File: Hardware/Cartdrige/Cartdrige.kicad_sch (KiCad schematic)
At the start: 5 parts, among them J1 CARTDRIGE, U1 28C256, U2 28C256

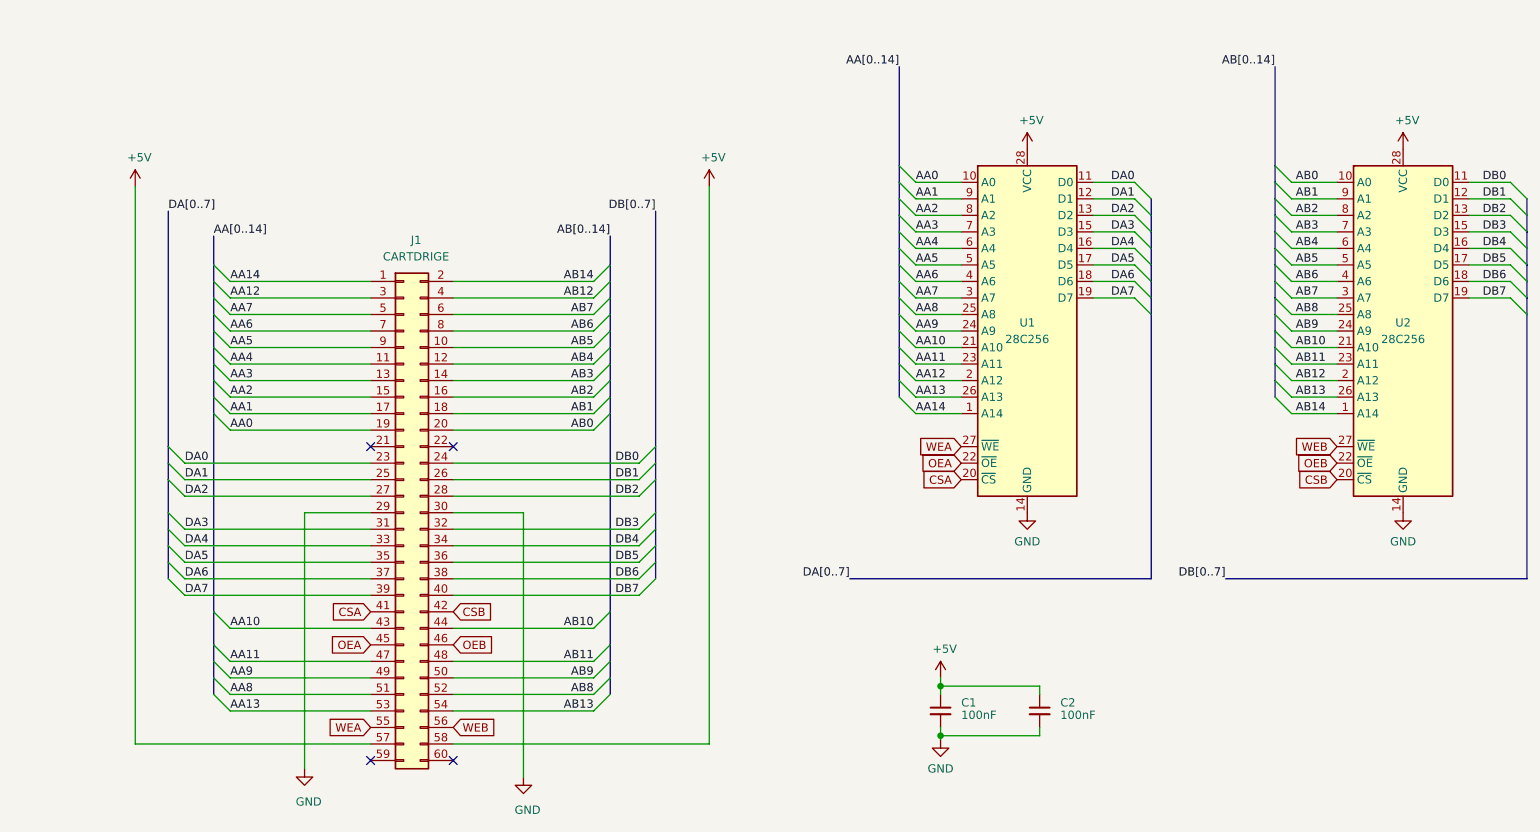
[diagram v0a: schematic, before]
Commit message: implement graphic loading from ROM
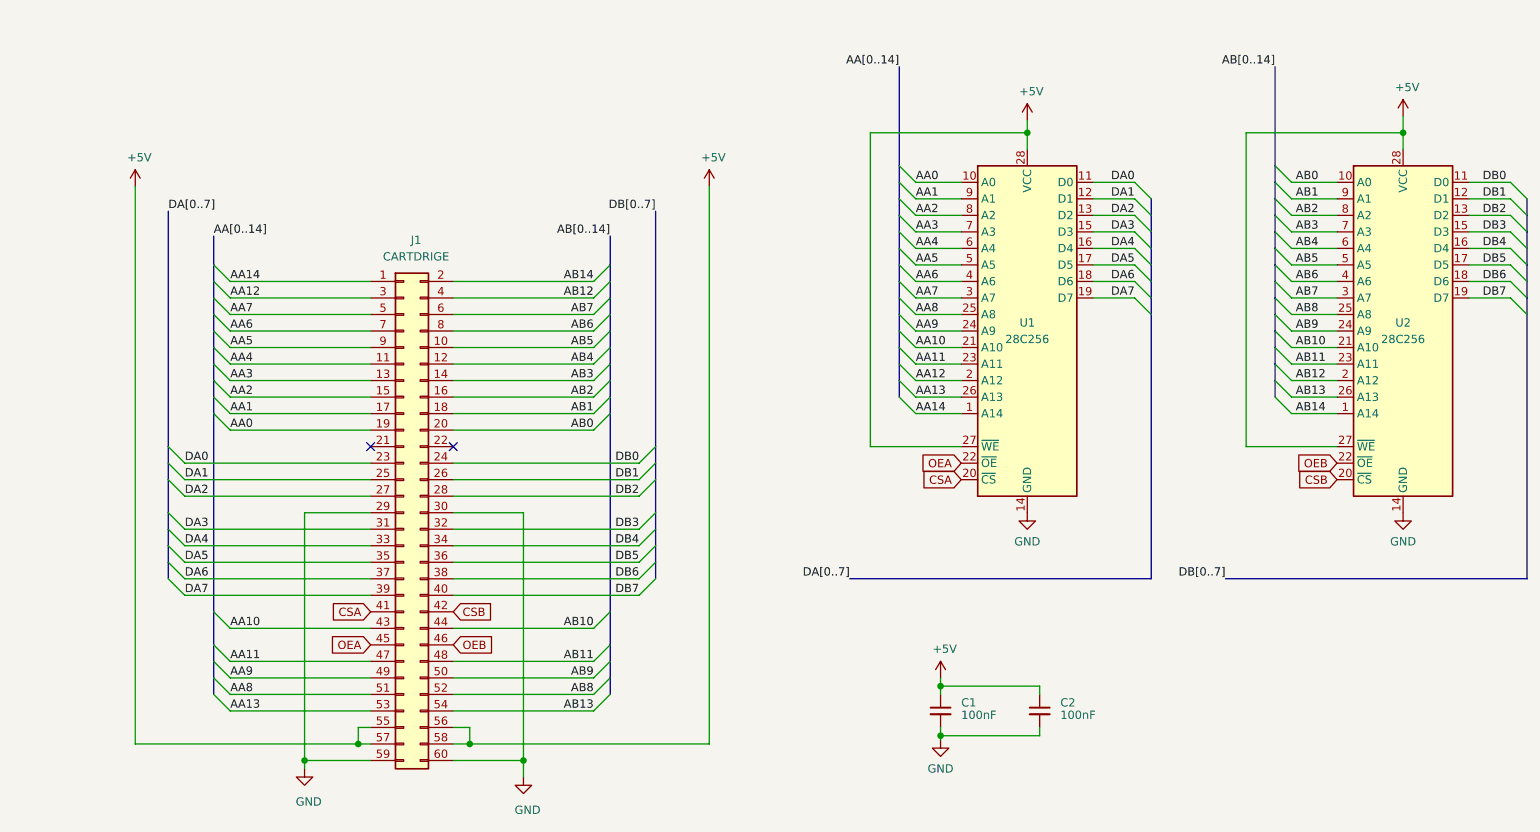
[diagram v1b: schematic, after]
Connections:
- net WEA is gone; now on net +5V: J1.55 (Pin_55), U1.27 (~WE)
- net WEB is gone; now on net +5V: J1.56 (Pin_56), U2.27 (~WE)
- net GND: now also J1.59 (Pin_59), J1.60 (Pin_60)
- no-connect marks 4 -> 2
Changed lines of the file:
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@@
 (kicad_sch (version 20201015) (generator eeschema)
   (paper "A4")
+  (junction (at 65.405 131.445) (diameter 1.016) (color 0 0 0 0))
+  (junction (at 73.66 128.905) (diameter 1.016) (color 0 0 0 0))
+  (junction (at 90.805 128.905) (diameter 1.016) (color 0 0 0 0))
+  (junction (at 99.06 131.445) (diameter 1.016) (color 0 0 0 0))
   (junction (at 163.195 120.015) (diameter 1.016) (color 0 0 0 0))
   (junction (at 163.195 127.635) (diameter 1.016) (color 0 0 0 0))
+  (junction (at 176.53 34.925) (diameter 1.016) (color 0 0 0 0))
+  (junction (at 234.315 34.925) (diameter 1.016) (color 0 0 0 0))
+  (no_connect (at 88.265 83.185))
   (no_connect (at 75.565 83.185))
-  (no_connect (at 88.265 83.185))
-  (no_connect (at 88.265 131.445))
-  (no_connect (at 75.565 131.445))
   (bus_entry (at 46.99 85.725) (size -2.54 -2.54)
     (stroke (width 0.1524) (type solid) (color 0 0 0 0))
@@
     (stroke (width 0) (type solid) (color 0 0 0 0))
   )
-  (wire (pts (xy 39.37 128.905) (xy 75.565 128.905))
+  (wire (pts (xy 39.37 128.905) (xy 73.66 128.905))
     (stroke (width 0) (type solid) (color 0 0 0 0))
   )
@@
     (stroke (width 0) (type solid) (color 0 0 0 0))
   )
-  (wire (pts (xy 65.405 93.345) (xy 65.405 132.715))
+  (wire (pts (xy 65.405 93.345) (xy 65.405 131.445))
     (stroke (width 0) (type solid) (color 0 0 0 0))
   )
@@
     (stroke (width 0) (type solid) (color 0 0 0 0))
   )
+  (wire (pts (xy 65.405 131.445) (xy 65.405 132.715))
+    (stroke (width 0) (type solid) (color 0 0 0 0))
+  )
+  (wire (pts (xy 65.405 131.445) (xy 75.565 131.445))
+    (stroke (width 0) (type solid) (color 0 0 0 0))
+  )
+  (wire (pts (xy 73.66 126.365) (xy 73.66 128.905))
+    (stroke (width 0) (type solid) (color 0 0 0 0))
+  )
+  (wire (pts (xy 73.66 128.905) (xy 75.565 128.905))
+    (stroke (width 0) (type solid) (color 0 0 0 0))
+  )
+  (wire (pts (xy 75.565 126.365) (xy 73.66 126.365))
+    (stroke (width 0) (type solid) (color 0 0 0 0))
+  )
   (wire (pts (xy 88.265 57.785) (xy 109.855 57.785))
     (stroke (width 0) (type solid) (color 0 0 0 0))
@@
     (stroke (width 0) (type solid) (color 0 0 0 0))
   )
-  (wire (pts (xy 88.265 128.905) (xy 127.635 128.905))
-    (stroke (width 0) (type solid) (color 0 0 0 0))
-  )
-  (wire (pts (xy 99.06 93.345) (xy 99.06 133.985))
+  (wire (pts (xy 88.265 126.365) (xy 90.805 126.365))
+    (stroke (width 0) (type solid) (color 0 0 0 0))
+  )
+  (wire (pts (xy 88.265 128.905) (xy 90.805 128.905))
+    (stroke (width 0) (type solid) (color 0 0 0 0))
+  )
+  (wire (pts (xy 88.265 131.445) (xy 99.06 131.445))
+    (stroke (width 0) (type solid) (color 0 0 0 0))
+  )
+  (wire (pts (xy 90.805 126.365) (xy 90.805 128.905))
+    (stroke (width 0) (type solid) (color 0 0 0 0))
+  )
+  (wire (pts (xy 90.805 128.905) (xy 127.635 128.905))
+    (stroke (width 0) (type solid) (color 0 0 0 0))
+  )
+  (wire (pts (xy 99.06 93.345) (xy 99.06 131.445))
+    (stroke (width 0) (type solid) (color 0 0 0 0))
+  )
+  (wire (pts (xy 99.06 131.445) (xy 99.06 133.985))
     (stroke (width 0) (type solid) (color 0 0 0 0))
   )
@@
     (stroke (width 0) (type solid) (color 0 0 0 0))
   )
+  (wire (pts (xy 152.4 34.925) (xy 176.53 34.925))
+    (stroke (width 0) (type solid) (color 0 0 0 0))
+  )
+  (wire (pts (xy 152.4 83.185) (xy 152.4 34.925))
+    (stroke (width 0) (type solid) (color 0 0 0 0))
+  )
   (wire (pts (xy 159.385 42.545) (xy 166.37 42.545))
     (stroke (width 0) (type solid) (color 0 0 0 0))
@@
     (stroke (width 0) (type solid) (color 0 0 0 0))
   )
+  (wire (pts (xy 166.37 83.185) (xy 152.4 83.185))
+    (stroke (width 0) (type solid) (color 0 0 0 0))
+  )
+  (wire (pts (xy 176.53 33.02) (xy 176.53 34.925))
+    (stroke (width 0) (type solid) (color 0 0 0 0))
+  )
+  (wire (pts (xy 176.53 34.925) (xy 176.53 37.465))
+    (stroke (width 0) (type solid) (color 0 0 0 0))
+  )
   (wire (pts (xy 178.435 120.015) (xy 163.195 120.015))
     (stroke (width 0) (type solid) (color 0 0 0 0))
@@
     (stroke (width 0) (type solid) (color 0 0 0 0))
   )
+  (wire (pts (xy 210.185 34.925) (xy 234.315 34.925))
+    (stroke (width 0) (type solid) (color 0 0 0 0))
+  )
+  (wire (pts (xy 210.185 83.185) (xy 210.185 34.925))
+    (stroke (width 0) (type solid) (color 0 0 0 0))
+  )
   (wire (pts (xy 217.17 42.545) (xy 224.155 42.545))
     (stroke (width 0) (type solid) (color 0 0 0 0))
@@
   )
   (wire (pts (xy 217.17 78.105) (xy 224.155 78.105))
+    (stroke (width 0) (type solid) (color 0 0 0 0))
+  )
+  (wire (pts (xy 224.155 83.185) (xy 210.185 83.185))
+    (stroke (width 0) (type solid) (color 0 0 0 0))
+  )
+  (wire (pts (xy 234.315 32.385) (xy 234.315 34.925))
+    (stroke (width 0) (type solid) (color 0 0 0 0))
+  )
+  (wire (pts (xy 234.315 34.925) (xy 234.315 37.465))
     (stroke (width 0) (type solid) (color 0 0 0 0))
   )
@@
     (effects (font (size 1.27 1.27)) (justify right))
   )
-  (global_label "WEA" (shape input) (at 75.565 126.365 180)    (property "Intersheet References" "${INTERSHEET_REFS}" (id 0) (at 67.9389 126.2856 0)
-      (effects (font (size 1.27 1.27)) (justify right) hide)
-    )
-    (effects (font (size 1.27 1.27)) (justify right))
-  )
   (global_label "CSB" (shape input) (at 88.265 108.585 0)    (property "Intersheet References" "${INTERSHEET_REFS}" (id 0) (at 95.9516 108.6644 0)
       (effects (font (size 1.27 1.27)) (justify left) hide)
@@
     (effects (font (size 1.27 1.27)) (justify left))
   )
-  (global_label "WEB" (shape input) (at 88.265 126.365 0)    (property "Intersheet References" "${INTERSHEET_REFS}" (id 0) (at 96.0726 126.4444 0)
-      (effects (font (size 1.27 1.27)) (justify left) hide)
-    )
-    (effects (font (size 1.27 1.27)) (justify left))
-  )
-  (global_label "WEA" (shape input) (at 166.37 83.185 180)    (property "Intersheet References" "${INTERSHEET_REFS}" (id 0) (at 158.7439 83.1056 0)
-      (effects (font (size 1.27 1.27)) (justify right) hide)
-    )
-    (effects (font (size 1.27 1.27)) (justify right))
-  )
   (global_label "OEA" (shape input) (at 166.37 85.725 180)    (property "Intersheet References" "${INTERSHEET_REFS}" (id 0) (at 158.8648 85.6456 0)
       (effects (font (size 1.27 1.27)) (justify right) hide)
@@
   )
   (global_label "CSA" (shape input) (at 166.37 88.265 180)    (property "Intersheet References" "${INTERSHEET_REFS}" (id 0) (at 158.8648 88.1856 0)
-      (effects (font (size 1.27 1.27)) (justify right) hide)
-    )
-    (effects (font (size 1.27 1.27)) (justify right))
-  )
-  (global_label "WEB" (shape input) (at 224.155 83.185 180)    (property "Intersheet References" "${INTERSHEET_REFS}" (id 0) (at 216.3474 83.1056 0)
       (effects (font (size 1.27 1.27)) (justify right) hide)
     )
@@
     )
   )
-  (symbol (lib_id "power:+5V") (at 176.53 37.465 0) (unit 1)
+  (symbol (lib_id "power:+5V") (at 176.53 33.02 0) (unit 1)
     (in_bom yes) (on_board yes)
-    (property "Reference" "#PWR0104" (id 0) (at 176.53 41.275 0)
-      (effects (font (size 1.27 1.27)) hide)
-    )
-    (property "Value" "+5V" (id 1) (at 177.165 33.02 0))
-    (property "Footprint" "" (id 2) (at 176.53 37.465 0)
-      (effects (font (size 1.27 1.27)) hide)
-    )
-    (property "Datasheet" "" (id 3) (at 176.53 37.465 0)
-      (effects (font (size 1.27 1.27)) hide)
-    )
-  )
-  (symbol (lib_id "power:+5V") (at 234.315 37.465 0) (unit 1)
+    (property "Reference" "#PWR0104" (id 0) (at 176.53 36.83 0)
+      (effects (font (size 1.27 1.27)) hide)
+    )
+    (property "Value" "+5V" (id 1) (at 177.165 28.575 0))
+    (property "Footprint" "" (id 2) (at 176.53 33.02 0)
+      (effects (font (size 1.27 1.27)) hide)
+    )
+    (property "Datasheet" "" (id 3) (at 176.53 33.02 0)
+      (effects (font (size 1.27 1.27)) hide)
+    )
+  )
+  (symbol (lib_id "power:+5V") (at 234.315 32.385 0) (unit 1)
     (in_bom yes) (on_board yes)
-    (property "Reference" "#PWR0103" (id 0) (at 234.315 41.275 0)
-      (effects (font (size 1.27 1.27)) hide)
-    )
-    (property "Value" "+5V" (id 1) (at 234.95 33.02 0))
-    (property "Footprint" "" (id 2) (at 234.315 37.465 0)
-      (effects (font (size 1.27 1.27)) hide)
-    )
-    (property "Datasheet" "" (id 3) (at 234.315 37.465 0)
-      (effects (font (size 1.27 1.27)) hide)
-    )
+    (property "Reference" "#PWR0103" (id 0) (at 234.315 36.195 0)
+      (effects (font (size 1.27 1.27)) hide)
+    )
+    (property "Value" "+5V" (id 1) (at 234.95 27.94 0))
+    (property "Footprint" "" (id 2) (at 234.315 32.385 0)
+      (effects (font (size 1.27 1.27)) hide)
+    )
+    (property "Datasheet" "" (id 3) (at 234.315 32.385 0)
+      (effects (font (size 1.27 1.27)) hide)
+    )

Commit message: Fix
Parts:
- removed C1, C2: 100nF, Capacitor_THT:C_Disc_D5.0mm_W2.5mm_P2.50mm, symbol Device:C_Small
- removed J1: CARTDRIGE, Connector_PCBEdge:Samtec_MECF-30-0_-L-DV_2x30_P1.27mm_Polarized_Edge, symbol Connector_Generic:Conn_02x30_Odd_Even
- removed U2: 28C256, Socket:DIP_Socket-28_W11.9_W12.7_W15.24_W17.78_W18.5_3M_228-1277-00-0602J, symbol Memory_EEPROM:28C256
- added C1: 100nF, Capacitor_THT:C_Disc_D5.0mm_W2.5mm_P2.50mm, symbol Device:C
- added J1: ROM, Connector_TheRLab:NES_PCBEdge, symbol Connector_Generic:Conn_02x15_Counter_Clockwise
- U1: footprint Socket:DIP_Socket-28_W11.9_W12.7_W15.24_W17.78_W18.5_3M_228-1277-00-0602J -> Package_DIP:DIP-28_W15.24mm
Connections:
- net +5V: now also C1.1, J1.27 (Pin_27), J1.28 (Pin_28)
- net GND: now also C1.2, J1.14 (Pin_14), J1.29 (Pin_29), J1.30 (Pin_30)
- net AA0 renamed A0
- net A0: now also J1.10 (Pin_10)
- net AA1 renamed A1
- net A1: now also J1.9 (Pin_9)
- net AA10 renamed A10
- net A10: now also J1.21 (Pin_21)
- net AA11 renamed A11
- net A11: now also J1.23 (Pin_23)
- net AA12 renamed A12
- net A12: now also J1.2 (Pin_2)
- net AA13 renamed A13
- net A13: now also J1.26 (Pin_26)
- net AA14 renamed A14
- net A14: now also J1.1 (Pin_1)
- net AA2 renamed A2
- net A2: now also J1.8 (Pin_8)
- net AA3 renamed A3
- net A3: now also J1.7 (Pin_7)
- net AA4 renamed A4
- net A4: now also J1.6 (Pin_6)
- net AA5 renamed A5
- net A5: now also J1.5 (Pin_5)
- net AA6 renamed A6
- net A6: now also J1.4 (Pin_4)
- net AA7 renamed A7
- net A7: now also J1.3 (Pin_3)
- net AA8 renamed A8
- net A8: now also J1.25 (Pin_25)
- net AA9 renamed A9
- net A9: now also J1.24 (Pin_24)
- net CSA renamed CS
- net CS: now also J1.20 (Pin_20)
- net DA0 renamed D0
- net D0: now also J1.11 (Pin_11)
- net DA1 renamed D1
- net D1: now also J1.12 (Pin_12)
- net DA2 renamed D2
- net D2: now also J1.13 (Pin_13)
- net DA3 renamed D3
- net D3: now also J1.15 (Pin_15)
- net DA4 renamed D4
- net D4: now also J1.16 (Pin_16)
- net DA5 renamed D5
- net D5: now also J1.17 (Pin_17)
- net DA6 renamed D6
- net D6: now also J1.18 (Pin_18)
- net DA7 renamed D7
- net D7: now also J1.19 (Pin_19)
- net OEA renamed OE
- net OE: now also J1.22 (Pin_22)
- no-connect marks 2 -> 0

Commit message: Finalize 1.3
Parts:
- removed J1: ROM, Connector_TheRLab:NES_PCBEdge, symbol Connector_Generic:Conn_02x15_Counter_Clockwise
- added J2: PORT1, NESConnector:NES_PCBEdge, symbol Connector_Generic:Conn_02x30_Odd_Even
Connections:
- net OE is gone; now on net GND: U1.22 (~{OE})
- net +5V: now also J2.2 (Pin_2), J2.59 (Pin_59)
- net A0: now also J2.25 (Pin_25)
- net A1: now also J2.23 (Pin_23)
- net A10: now also J2.5 (Pin_5)
- net A11: now also J2.3 (Pin_3)
- net A12: now also J2.6 (Pin_6)
- net A13: now also J2.8 (Pin_8)
- net A14: now also J2.10 (Pin_10)
- net A2: now also J2.21 (Pin_21)
- net A3: now also J2.19 (Pin_19)
- net A4: now also J2.17 (Pin_17)
- net A5: now also J2.15 (Pin_15)
- net A6: now also J2.13 (Pin_13)
- net A7: now also J2.11 (Pin_11)
- net A8: now also J2.9 (Pin_9)
- net A9: now also J2.7 (Pin_7)
- net D0: now also J2.28 (Pin_28)
- net D1: now also J2.26 (Pin_26)
- net D2: now also J2.24 (Pin_24)
- net D3: now also J2.22 (Pin_22)
- net D4: now also J2.20 (Pin_20)
- net D5: now also J2.18 (Pin_18)
- net D6: now also J2.16 (Pin_16)
- net D7: now also J2.14 (Pin_14)
- net GND: now also J2.1 (Pin_1), J2.31 (Pin_31)
- net CS renamed PORT1CSB
- net PORT1CSB: now also J2.30 (Pin_30)
- new net A15: J2.12 (Pin_12)
- new net CLOCK: J2.4 (Pin_4)
- new net DMAB: J2.34 (Pin_34)
- new net IRQ3B: J2.29 (Pin_29)
- new net NMIB: J2.36 (Pin_36)
- new net RAMCSB: J2.33 (Pin_33)
- new net RESET: J2.32 (Pin_32)
- new net RW: J2.27 (Pin_27)
- no-connect marks 0 -> 24
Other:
- moved on the sheet: C1, U1
